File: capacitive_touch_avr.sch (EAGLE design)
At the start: 13 parts

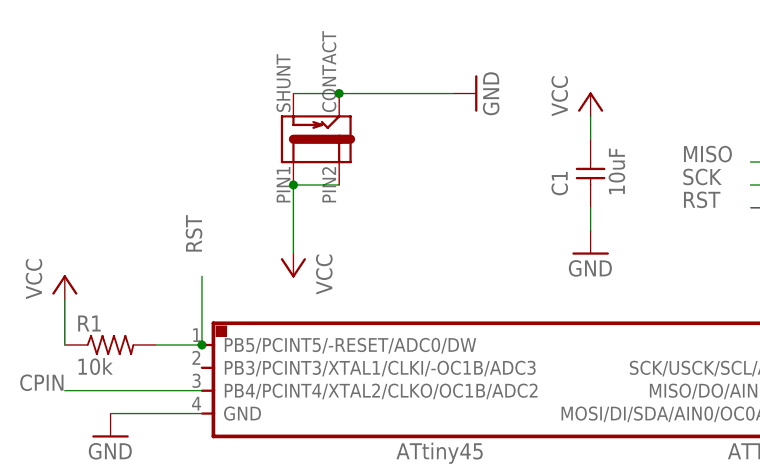
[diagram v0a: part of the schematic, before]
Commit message: Tested and working version Modifying power jack from SMD to TH
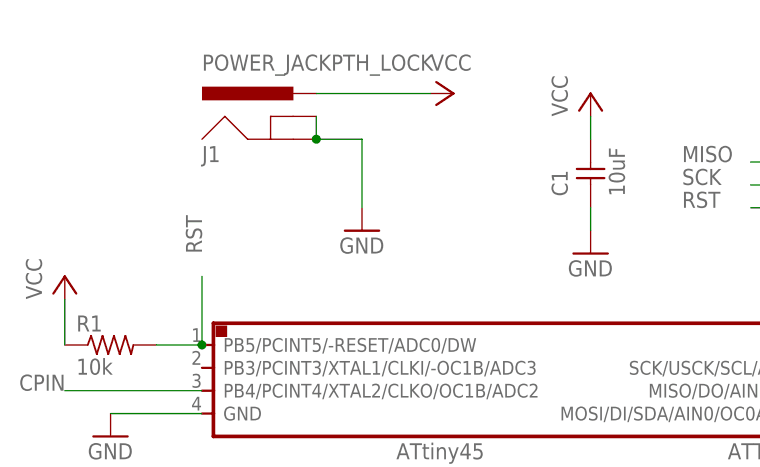
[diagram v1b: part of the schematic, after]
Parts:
- removed POWER: JACK-2.1MM, fab:JACK-2.1MM
- added J1: POWER_JACKPTH_LOCK, SparkFun-Connectors:POWER_JACKPTH_LOCK
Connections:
- net GND: now also J1.GND, J1.GNDBREAK; no longer POWER.CONTACT, POWER.SHUNT
- net VCC: now also J1.PWR; no longer POWER.PIN1, POWER.PIN2
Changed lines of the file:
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@@
 <layer number="230" name="230bmp" color="7" fill="1" visible="no" active="yes"/>
 <layer number="231" name="231bmp" color="7" fill="1" visible="no" active="yes"/>
+<layer number="232" name="Eagle3D_PG2" color="7" fill="1" visible="yes" active="yes"/>
+<layer number="233" name="Eagle3D_PG3" color="7" fill="1" visible="yes" active="yes"/>
 <layer number="248" name="Housing" color="7" fill="1" visible="no" active="yes"/>
 <layer number="249" name="Edge" color="7" fill="1" visible="no" active="yes"/>
@@
 <part name="GND7" library="supply1" library_urn="urn:adsk.eagle:library:371" deviceset="GND" device=""/>
 <part name="P+7" library="supply1" library_urn="urn:adsk.eagle:library:371" deviceset="VCC" device=""/>
-<part name="POWER" library="fab" deviceset="JACK-2.1MM" device=""/>
 <part name="ISP" library="fab" deviceset="AVRISP" device="SMD"/>
 <part name="JUMR" library="fab" deviceset="SOLDER_JUMPER" device=""/>
 <part name="JUM0" library="fab" deviceset="SOLDER_JUMPER" device=""/>
+<part name="J1" library="SparkFun-Connectors" library_urn="urn:adsk.eagle:library:513" deviceset="POWER_JACK" device="PTH_LOCK" package3d_urn="urn:adsk.eagle:package:38224/1"/>
 </parts>
 <sheets>
@@
 <instance part="GND6" gate="1" x="76.2" y="12.7"/>
 <instance part="P+6" gate="VCC" x="104.14" y="25.4"/>
-<instance part="GND7" gate="1" x="45.72" y="78.74" rot="R90"/>
-<instance part="P+7" gate="VCC" x="25.4" y="58.42" rot="R180"/>
-<instance part="POWER" gate="G$1" x="27.94" y="73.66" rot="R90"/>
+<instance part="GND7" gate="1" x="33.02" y="63.5"/>
+<instance part="P+7" gate="VCC" x="43.18" y="78.74" rot="R270"/>
 <instance part="ISP" gate="G$1" x="86.36" y="68.58"/>
 <instance part="JUMR" gate="G$1" x="30.48" y="17.78" rot="R90"/>
 <instance part="JUM0" gate="G$1" x="38.1" y="17.78" rot="R90"/>
+<instance part="J1" gate="G$1" x="25.4" y="71.12"/>
 </instances>
 <busses>
@@
 </segment>
 <segment>
+<pinref part="J1" gate="G$1" pin="PWR"/>
 <pinref part="P+7" gate="VCC" pin="VCC"/>
-<pinref part="POWER" gate="G$1" pin="PIN1"/>
-<wire x1="25.4" y1="68.58" x2="25.4" y2="60.96" width="0.1524" layer="91"/>
-<pinref part="POWER" gate="G$1" pin="PIN2"/>
-<wire x1="30.48" y1="68.58" x2="25.4" y2="68.58" width="0.1524" layer="91"/>
-<junction x="25.4" y="68.58"/>
+<wire x1="27.94" y1="78.74" x2="40.64" y2="78.74" width="0.1524" layer="91"/>
 </segment>
 </net>
@@
 </segment>
 <segment>
+<pinref part="J1" gate="G$1" pin="GNDBREAK"/>
+<pinref part="J1" gate="G$1" pin="GND"/>
+<wire x1="27.94" y1="76.2" x2="27.94" y2="73.66" width="0.1524" layer="91"/>
 <pinref part="GND7" gate="1" pin="GND"/>
-<pinref part="POWER" gate="G$1" pin="CONTACT"/>
-<wire x1="43.18" y1="78.74" x2="30.48" y2="78.74" width="0.1524" layer="91"/>
-<pinref part="POWER" gate="G$1" pin="SHUNT"/>
-<wire x1="25.4" y1="78.74" x2="30.48" y2="78.74" width="0.1524" layer="91"/>
-<junction x="30.48" y="78.74"/>
+<wire x1="33.02" y1="66.04" x2="33.02" y2="73.66" width="0.1524" layer="91"/>
+<wire x1="33.02" y1="73.66" x2="27.94" y2="73.66" width="0.1524" layer="91"/>
+<junction x="27.94" y="73.66"/>
 </segment>
 </net>
@@
 will not be understood (or retained) with this version.
 </note>
+<note version="8.3" severity="warning">
+Since Version 8.3, EAGLE supports the association of 3D packages
+with devices in libraries, schematics, and board files. Those 3D
+packages will not be understood (or retained) with this version.
+</note>
 </compatibility>
